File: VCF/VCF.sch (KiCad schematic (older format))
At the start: 33 parts, among them J1 Env, J2 Power, J3 Output, J4 Input, U1 LM324A

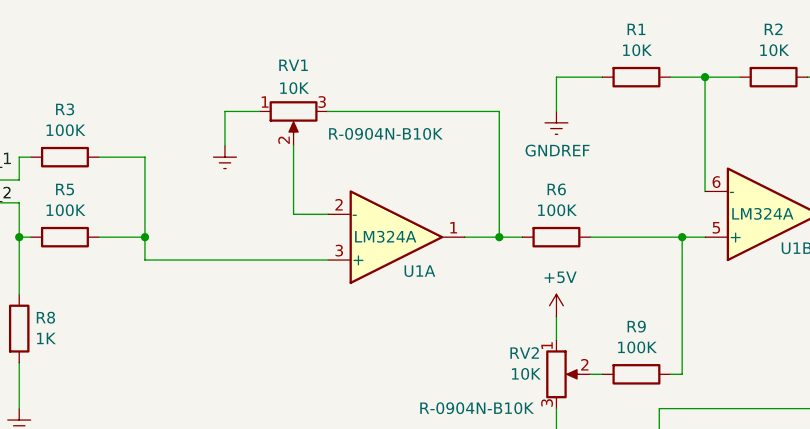
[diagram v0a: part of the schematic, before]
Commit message: New edit schems, add net lists, pcb files and library
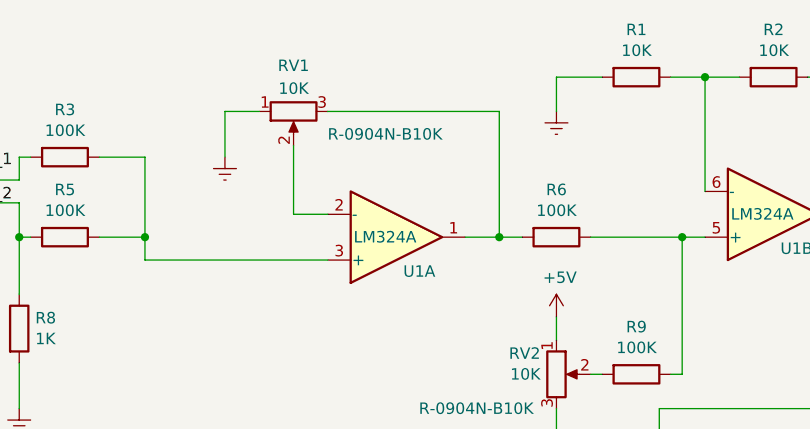
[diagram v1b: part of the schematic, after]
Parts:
- RV1, RV2, RV3: footprint Potentiometer_THT:Potentiometer_Bourns_PTV09A-1_Single_Vertical -> R0409N:PTV09A4020FB103
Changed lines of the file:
@@
 EESchema Schematic File Version 4
-LIBS:VCF-cache
 EELAYER 26 0
 EELAYER END
@@
 F 0 "RV1" V 3150 1100 50  0000 C CNN
 F 1 "10K" V 3250 1100 50  0000 C CNN
-F 2 "Potentiometer_THT:Potentiometer_Bourns_PTV09A-1_Single_Vertical" H 3350 1100 50  0001 C CNN
+F 2 "R0409N:PTV09A4020FB103" H 3350 1100 50  0001 C CNN
 F 3 "~" H 3350 1100 50  0001 C CNN
 F 4 "R-0904N-B10K" V 3450 700 50  0000 C CNN "Тип"
@@
 L power:GNDREF #PWR02
 U 1 1 5C969560
-P 3050 1250
-F 0 "#PWR02" H 3050 1000 50  0001 C CNN
-F 1 "GNDREF" H 3055 1077 50  0001 C CNN
-F 2 "" H 3050 1250 50  0001 C CNN
-F 3 "" H 3050 1250 50  0001 C CNN
-	1    3050 1250
+P 3050 1300
+F 0 "#PWR02" H 3050 1050 50  0001 C CNN
+F 1 "GNDREF" H 3055 1127 50  0001 C CNN
+F 2 "" H 3050 1300 50  0001 C CNN
+F 3 "" H 3050 1300 50  0001 C CNN
+	1    3050 1300
 	1    0    0    -1
 $EndComp
 Wire Wire Line
 	3200 1100 3050 1100
-Wire Wire Line
-	3050 1100 3050 1250
 $Comp
 L Amplifier_Operational:LM324A U1
@@
 F 0 "RV2" H 4430 2341 50  0000 R CNN
 F 1 "10K" H 4430 2250 50  0000 R CNN
-F 2 "Potentiometer_THT:Potentiometer_Bourns_PTV09A-1_Single_Vertical" H 4500 2250 50  0001 C CNN
+F 2 "R0409N:PTV09A4020FB103" H 4500 2250 50  0001 C CNN
 F 3 "~" H 4500 2250 50  0001 C CNN
 F 4 "R-0904N-B10K" H 4400 2100 50  0000 R CNN "Тип"
@@
 P 4500 1100
 F 0 "#PWR01" H 4500 850 50  0001 C CNN
-F 1 "GNDREF" H 4505 927 50  0000 C CNN
+F 1 "GNDREF" H 4505 927 50  0001 C CNN
 F 2 "" H 4500 1100 50  0001 C CNN
 F 3 "" H 4500 1100 50  0001 C CNN
@@
 F 0 "RV3" V 5435 3650 50  0000 C CNN
 F 1 "10K" V 5344 3650 50  0000 C CNN
-F 2 "Potentiometer_THT:Potentiometer_Bourns_PTV09A-1_Single_Vertical" H 5550 3650 50  0001 C CNN
+F 2 "R0409N:PTV09A4020FB103" H 5550 3650 50  0001 C CNN
 F 3 "~" H 5550 3650 50  0001 C CNN
 F 4 "R-0904N-B10K" V 5850 3500 50  0000 C CNN "Тип"
@@
 Text Label 2000 4800 0    50   ~ 0
 IN_2
+Wire Wire Line
+	3050 1100 3050 1300
 $EndSCHEMATC

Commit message: Изменены библиотеки. Добавлинны библиотеки примененные в проекте локально. Добавленны заготовки для печатных плат. Добавленны 3D модели компоненток.
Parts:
- C1, C2, C3, C4: footprint Capacitor_SMD:C_0603_1608Metric -> footprint:c0603; symbol Device:C -> uRack:C
- D1: footprint Diode_SMD:D_0603_1608Metric -> footprint:d0603; symbol Device:D -> uRack:D
- J1, J4: footprint Connector_PinHeader_2.54mm:PinHeader_1x02_P2.54mm_Vertical -> footprint:pls1x02; symbol Connector:Conn_01x02_Male -> uRack:Conn_01x02_Male
- J2, J3: footprint Connector_PinHeader_2.54mm:PinHeader_1x03_P2.54mm_Vertical -> footprint:pls1x03; symbol Connector:Conn_01x03_Male -> uRack:Conn_01x03_Male
- R1, R10, R11, R12, R13, R14, R15, R16, R17, R18, R19, R2, R20, R3, R4, R5, R6, R7, R8, R9: footprint Resistor_SMD:R_0603_1608Metric -> footprint:r0603; symbol Device:R -> uRack:R
- RV1, RV2, RV3: footprint R0409N:PTV09A4020FB103 -> footprint:PTV09A4020FB103; symbol Device:R_POT -> uRack:R_POT
- U1: footprint Package_SO:SOIC-14_3.9x8.7mm_P1.27mm -> footprint:soic-14; symbol Amplifier_Operational:LM324A -> uRack:LM324
